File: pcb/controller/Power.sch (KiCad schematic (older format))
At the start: 4 parts

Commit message: controller schematic capture almost done
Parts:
- added C? (x3): 10u, symbol Device:C
- added C?: 47u, symbol Device:C
- added C? (x2): C, symbol Device:C
- added C? (x2): 10n, symbol Device:C
- added C? (x4): 4.7u, symbol Device:C
- added L?: L, symbol Device:L
- added R? (x7): R, symbol Device:R
- added U?: LMZ14201, symbol wbraun_ic_lib:LMZ14201
- added U? (x2): TPS735, symbol wbraun_ic_lib:TPS735
- added U?: TPS82084, symbol wbraun_ic_lib:TPS82084
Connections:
- net at FL?.1: now also J?.1 (Pin_1)
- net at FL?.2: now also C?.1, L?.1
- net at FL?.3: now also J?.2 (Pin_2)
- net GND: now reaches FL?.4
- net GND: now also C?.2, C?.2, C?.1, C?.1, C?.1, C?.1, C?.1, C?.1, C?.1, C?.2, C?.2, C?.2, C?.2, C?.2, R?.1, R?.1, R?.1, R?.2, R?.2, U?.4 (GND), U?.4 (GND), U?.4 (GND), U?.5 (GND), U?.6 (GND), U?.8 (GND), U?.9 (GND), U?.9 (GND), U?.9 (GND)
- net +24V: now reaches C?.1
- net +24V: now also C?.1, L?.2, R?.1, U?.1 (VIN)
- new net: R?.2, U?.2 (RON)
- new net: R?.1, R?.2, U?.3 (EN)
- new net: C?.1, U?.5 (SS)
- new net: C?.2, R?.1, R?.2, U?.6 (FB)
- new net: C?.2, U?.3 (NR/FB) (x2)
- new net: R?.1, R?.2, U?.7 (FB)
- new net +1V0: C?.1, R?.2, U?.8 (VOUT)
- new net +1V8: C?.2, U?.1 (OUT)
- new net +3V3: C?.2, U?.1 (OUT)
- new net +5V: C?.1, C?.1, C?.2, C?.2, U?.1 (EN), U?.3 (VIN), U?.4 (VIN), U?.5 (EN), U?.5 (EN), U?.7 (VOUT), U?.8 (IN), U?.8 (IN)
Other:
- moved on the sheet: C?, FL?

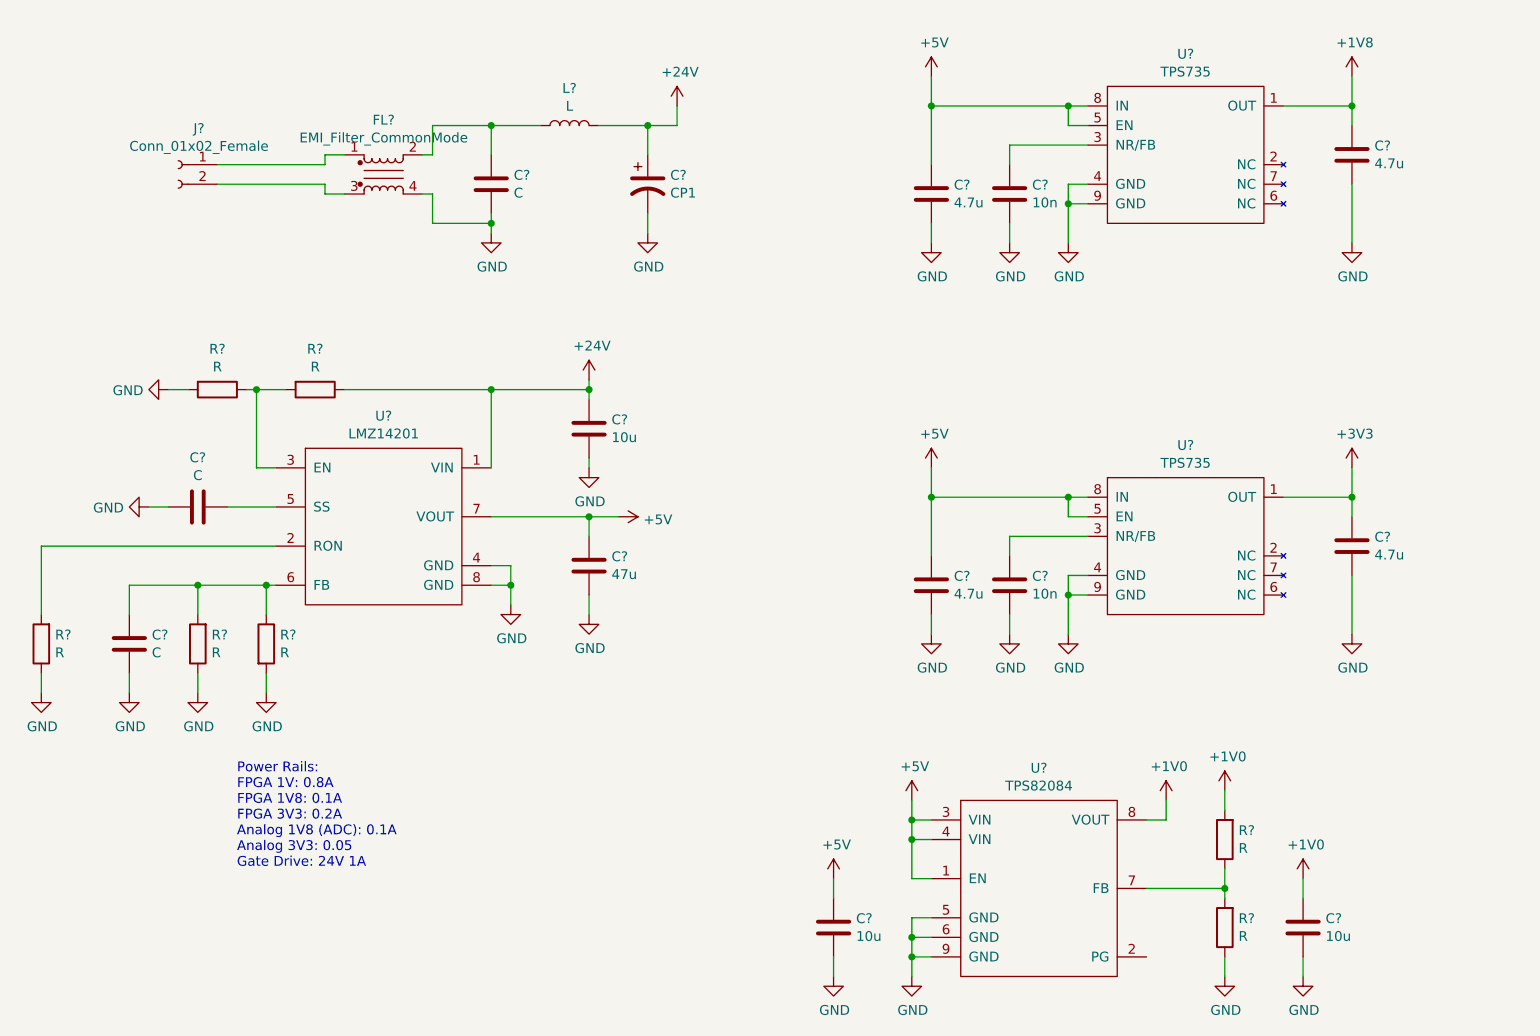
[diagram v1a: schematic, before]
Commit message: started assigning footprints
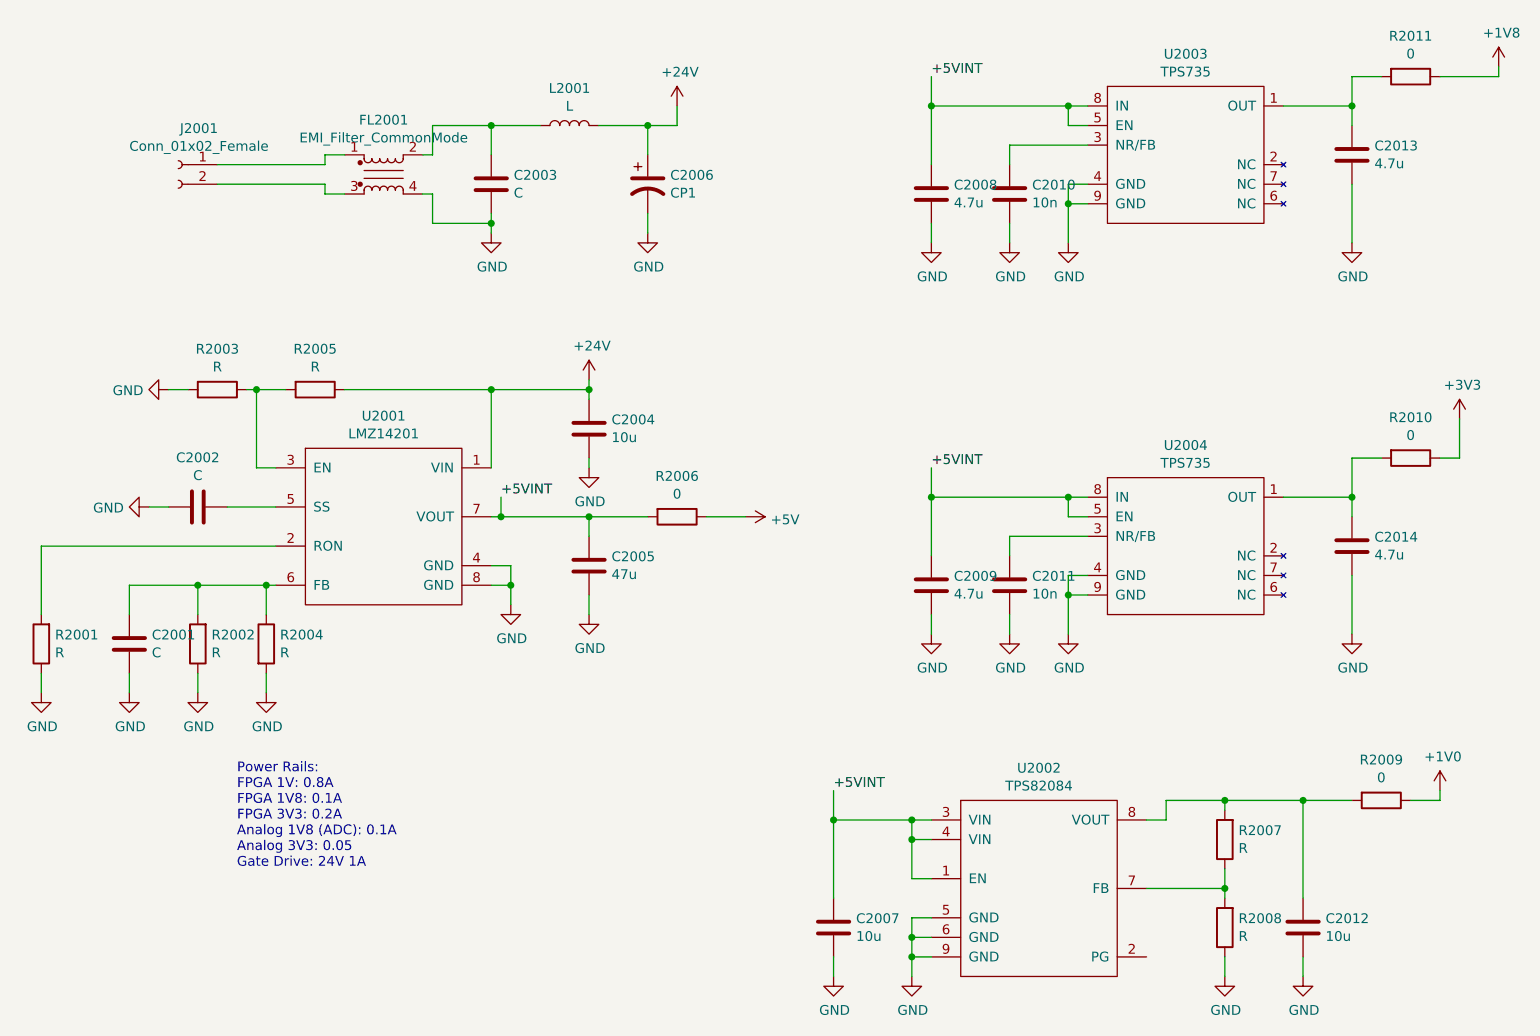
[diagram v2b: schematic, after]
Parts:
- added R2006, R2009, R2010, R2011: 0, symbol Device:R
- C2001, C2002, C2008, C2009, C2010, C2011, C2012, C2013, C2014: renamed from C?; footprint (none) -> Capacitor_SMD:C_0402_1005Metric
- C2004: renamed from C?; footprint (none) -> Capacitor_SMD:C_1206_3216Metric
- C2005, C2007: renamed from C?; footprint (none) -> Capacitor_SMD:C_0805_2012Metric
- gave numbers to parts that had none: 16
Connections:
- net +1V0: now also R2009.1; no longer C2012.1, R2007.2, U2002.8 (VOUT)
- net +1V8: now also R2011.1; no longer C2013.2, U2003.1 (OUT)
- net +3V3: now also R2010.1; no longer C2014.2, U2004.1 (OUT)
- net +5V: now also R2006.1; no longer C2005.1, C2007.1, C2008.2, C2009.2, U2001.7 (VOUT), U2002.1 (EN), U2002.3 (VIN), U2002.4 (VIN), U2003.5 (EN), U2003.8 (IN), U2004.5 (EN), U2004.8 (IN)
- new net: C2013.2, R2011.2, U2003.1 (OUT)
- new net: C2014.2, R2010.2, U2004.1 (OUT)
- new net: C2012.1, R2007.2, R2009.2, U2002.8 (VOUT)
- new net +5VINT: C2005.1, C2007.1, C2008.2, C2009.2, R2006.2, U2001.7 (VOUT), U2002.1 (EN), U2002.3 (VIN), U2002.4 (VIN), U2003.5 (EN), U2003.8 (IN), U2004.5 (EN), U2004.8 (IN)

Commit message: pcb component placement almost done
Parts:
- added C2015: CP2, wbraun_smd:CAP_16mmx37mm_horizontal, symbol Device:CP1
- C2003: footprint (none) -> Capacitor_SMD:C_0805_2012Metric
- C2006: footprint (none) -> Capacitor_THT:CP_Radial_D10.0mm_P5.00mm
- C2012: footprint Capacitor_SMD:C_0402_1005Metric -> Capacitor_SMD:C_0805_2012Metric
- FL2001: footprint (none) -> wbraun_smd:DLW5BTM
- J2001: footprint (none) -> wbraun_smd:TerminalBlock-5.0mm-2
- L2001: footprint (none) -> Inductor_SMD:L_Vishay_IHLP-1212
- R2001, R2002, R2003, R2004, R2005, R2007, R2008: footprint (none) -> Resistor_SMD:R_0402_1005Metric
- R2006, R2009, R2010, R2011: footprint (none) -> Resistor_SMD:R_0805_2012Metric
- U2001: footprint (none) -> wbraun_smd:TO-PMOD-7
- U2002: footprint (none) -> wbraun_smd:uSil-8
- U2003, U2004: footprint (none) -> wbraun_smd:SON-8_EP
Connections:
- net +24V: now also C2015.1
- net +5V: now also C2007.1, C2008.2, C2009.2, U2002.1 (EN), U2002.3 (VIN), U2002.4 (VIN), U2003.5 (EN), U2003.8 (IN), U2004.5 (EN), U2004.8 (IN)
- net +5VINT: now also C2001.1, R2002.1; no longer C2007.1, C2008.2, C2009.2, U2002.1 (EN), U2002.3 (VIN), U2002.4 (VIN), U2003.5 (EN), U2003.8 (IN), U2004.5 (EN), U2004.8 (IN)
- net GND: now also FL2001.3, C2015.2; no longer C2001.1, FL2001.4, R2002.1
- net at FL2001.1: now also C2003.1, L2001.1; no longer J2001.1 (Pin_1)
- net at J2001.2 (Pin_2): now also FL2001.4; no longer FL2001.3
- new net: FL2001.2, J2001.1 (Pin_1)
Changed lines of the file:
@@
 F 0 "FL2001" H 2500 2428 50  0000 C CNN
 F 1 "EMI_Filter_CommonMode" H 2500 2337 50  0000 C CNN
-F 2 "" V 2500 2190 50  0001 C CNN
+F 2 "wbraun_smd:DLW5BTM" V 2500 2190 50  0001 C CNN
 F 3 "~" V 2500 2190 50  0000 C CNN
 	1    2500 2150
-	1    0    0    -1
+	-1   0    0    -1
 $EndComp
 $Comp
@@
 F 0 "J2001" H 1344 2285 50  0000 C CNN
 F 1 "Conn_01x02_Female" H 1344 2194 50  0000 C CNN
-F 2 "" H 1450 2100 50  0001 C CNN
+F 2 "wbraun_smd:TerminalBlock-5.0mm-2" H 1450 2100 50  0001 C CNN
 F 3 "~" H 1450 2100 50  0001 C CNN
 	1    1450 2100
@@
 F 0 "C2003" H 3165 2246 50  0000 L CNN
 F 1 "C" H 3165 2155 50  0000 L CNN
-F 2 "" H 3088 2050 50  0001 C CNN
+F 2 "Capacitor_SMD:C_0805_2012Metric" H 3088 2050 50  0001 C CNN
 F 3 "~" H 3050 2200 50  0001 C CNN
 	1    3050 2200
@@
 F 0 "C2006" H 3965 2246 50  0000 L CNN
 F 1 "CP1" H 3965 2155 50  0000 L CNN
-F 2 "" H 3850 2200 50  0001 C CNN
+F 2 "Capacitor_THT:CP_Radial_D10.0mm_P5.00mm" H 3850 2200 50  0001 C CNN
 F 3 "~" H 3850 2200 50  0001 C CNN
 	1    3850 2200
@@
 F 0 "L2001" V 3640 1900 50  0000 C CNN
 F 1 "L" V 3549 1900 50  0000 C CNN
-F 2 "" H 3450 1900 50  0001 C CNN
+F 2 "Inductor_SMD:L_Vishay_IHLP-1212" H 3450 1900 50  0001 C CNN
 F 3 "~" H 3450 1900 50  0001 C CNN
 	1    3450 1900
@@
 F 0 "U2001" H 2500 4515 50  0000 C CNN
 F 1 "LMZ14201" H 2500 4424 50  0000 C CNN
-F 2 "" H 2100 3750 50  0001 C CNN
+F 2 "wbraun_smd:TO-PMOD-7" H 2100 3750 50  0001 C CNN
 F 3 "" H 2100 3750 50  0001 C CNN
 	1    2500 3950
@@
 F 0 "R2002" H 1480 4504 50  0000 R CNN
 F 1 "R" H 1480 4595 50  0000 R CNN
-F 2 "" V 1480 4550 50  0001 C CNN
+F 2 "Resistor_SMD:R_0402_1005Metric" V 1480 4550 50  0001 C CNN
 F 3 "~" H 1550 4550 50  0001 C CNN
 	1    1550 4550
@@
 F 0 "R2004" H 1970 4596 50  0000 L CNN
 F 1 "R" H 1970 4505 50  0000 L CNN
-F 2 "" V 1830 4550 50  0001 C CNN
+F 2 "Resistor_SMD:R_0402_1005Metric" V 1830 4550 50  0001 C CNN
 F 3 "~" H 1900 4550 50  0001 C CNN
 	1    1900 4550
@@
 F 0 "R2005" V 1943 3250 50  0000 C CNN
 F 1 "R" V 2034 3250 50  0000 C CNN
-F 2 "" V 2080 3250 50  0001 C CNN
+F 2 "Resistor_SMD:R_0402_1005Metric" V 2080 3250 50  0001 C CNN
 F 3 "~" H 2150 3250 50  0001 C CNN
 	1    2150 3250
@@
 F 0 "R2003" V 1443 3250 50  0000 C CNN
 F 1 "R" V 1534 3250 50  0000 C CNN
-F 2 "" V 1580 3250 50  0001 C CNN
+F 2 "Resistor_SMD:R_0402_1005Metric" V 1580 3250 50  0001 C CNN
 F 3 "~" H 1650 3250 50  0001 C CNN
 	1    1650 3250
@@
 F 0 "R2001" H 680 4504 50  0000 R CNN
 F 1 "R" H 680 4595 50  0000 R CNN
-F 2 "" V 680 4550 50  0001 C CNN
+F 2 "Resistor_SMD:R_0402_1005Metric" V 680 4550 50  0001 C CNN
 F 3 "~" H 750 4550 50  0001 C CNN
 	1    750  4550
@@
 $EndComp
 $Comp
-L power:GND #PWR0111
-U 1 1 5C6A74F1
-P 1200 4800
-F 0 "#PWR0111" H 1200 4550 50  0001 C CNN
-F 1 "GND" H 1205 4627 50  0000 C CNN
-F 2 "" H 1200 4800 50  0001 C CNN
-F 3 "" H 1200 4800 50  0001 C CNN
-	1    1200 4800
-	1    0    0    -1
-$EndComp
-$Comp
-L power:GND #PWR0112
-U 1 1 5C6A751A
-P 1550 4800
-F 0 "#PWR0112" H 1550 4550 50  0001 C CNN
-F 1 "GND" H 1555 4627 50  0000 C CNN
-F 2 "" H 1550 4800 50  0001 C CNN
-F 3 "" H 1550 4800 50  0001 C CNN
-	1    1550 4800
-	1    0    0    -1
-$EndComp
-$Comp
 L power:GND #PWR0113
 U 1 1 5C6A7543
@@
 F 0 "U2003" H 6600 2565 50  0000 C CNN
 F 1 "TPS735" H 6600 2474 50  0000 C CNN
-F 2 "" H 7300 1800 50  0001 C CNN
+F 2 "wbraun_smd:SON-8_EP" H 7300 1800 50  0001 C CNN
 F 3 "" H 7300 1800 50  0001 C CNN
 	1    6600 2050
@@
 F 0 "U2004" H 6600 4565 50  0000 C CNN
 F 1 "TPS735" H 6600 4474 50  0000 C CNN
-F 2 "" H 7300 3800 50  0001 C CNN
+F 2 "wbraun_smd:SON-8_EP" H 7300 3800 50  0001 C CNN
 F 3 "" H 7300 3800 50  0001 C CNN
 	1    6600 4050
@@
 F 0 "U2002" H 5850 6415 50  0000 C CNN
 F 1 "TPS82084" H 5850 6324 50  0000 C CNN
-F 2 "" H 5800 5800 50  0001 C CNN
+F 2 "wbraun_smd:uSil-8" H 5800 5800 50  0001 C CNN
 F 3 "" H 5800 5800 50  0001 C CNN
 	1    5850 5800
@@
 F 0 "C2012" H 7315 6046 50  0000 L CNN
 F 1 "10u" H 7315 5955 50  0000 L CNN
-F 2 "Capacitor_SMD:C_0402_1005Metric" H 7238 5850 50  0001 C CNN
+F 2 "Capacitor_SMD:C_0805_2012Metric" H 7238 5850 50  0001 C CNN
 F 3 "~" H 7200 6000 50  0001 C CNN
 	1    7200 6000
@@
 F 0 "R2007" H 6730 5504 50  0000 R CNN
 F 1 "R" H 6730 5595 50  0000 R CNN
-F 2 "" V 6730 5550 50  0001 C CNN
+F 2 "Resistor_SMD:R_0402_1005Metric" V 6730 5550 50  0001 C CNN
 F 3 "~" H 6800 5550 50  0001 C CNN
 	1    6800 5550
@@
 F 0 "R2008" H 6730 5954 50  0000 R CNN
 F 1 "R" H 6730 6045 50  0000 R CNN
-F 2 "" V 6730 6000 50  0001 C CNN
+F 2 "Resistor_SMD:R_0402_1005Metric" V 6730 6000 50  0001 C CNN
 F 3 "~" H 6800 6000 50  0001 C CNN
 	1    6800 6000
@@
 F 0 "R2006" V 3793 3900 50  0000 C CNN
 F 1 "0" V 3884 3900 50  0000 C CNN
-F 2 "" V 3930 3900 50  0001 C CNN
+F 2 "Resistor_SMD:R_0805_2012Metric" V 3930 3900 50  0001 C CNN
 F 3 "~" H 4000 3900 50  0001 C CNN
 	1    4000 3900
@@
 	4800 5450 4800 5300
 Connection ~ 4800 5450
-Text Label 4800 5300 0    50   ~ 0
-+5VINT
-Text Label 5300 3650 0    50   ~ 0
-+5VINT
-Text Label 5300 1650 0    50   ~ 0
-+5VINT
 $Comp
 L Device:R R2011
@@
 F 0 "R2011" V 7543 1650 50  0000 C CNN
 F 1 "0" V 7634 1650 50  0000 C CNN
-F 2 "" V 7680 1650 50  0001 C CNN
+F 2 "Resistor_SMD:R_0805_2012Metric" V 7680 1650 50  0001 C CNN
 F 3 "~" H 7750 1650 50  0001 C CNN
 	1    7750 1650
@@
 F 0 "R2010" V 7543 3600 50  0000 C CNN
 F 1 "0" V 7634 3600 50  0000 C CNN
-F 2 "" V 7680 3600 50  0001 C CNN
+F 2 "Resistor_SMD:R_0805_2012Metric" V 7680 3600 50  0001 C CNN
 F 3 "~" H 7750 3600 50  0001 C CNN
 	1    7750 3600
@@
 F 0 "R2009" V 7393 5350 50  0000 C CNN
 F 1 "0" V 7484 5350 50  0000 C CNN
-F 2 "" V 7530 5350 50  0001 C CNN
+F 2 "Resistor_SMD:R_0805_2012Metric" V 7530 5350 50  0001 C CNN
 F 3 "~" H 7600 5350 50  0001 C CNN
 	1    7600 5350
@@
 Wire Wire Line
 	8200 1650 7900 1650
+Text Label 1200 4800 0    50   ~ 0
++5VINT
+Text Label 1550 4800 0    50   ~ 0
++5VINT
+$Comp
+L Device:CP1 C2015
+U 1 1 5C5EEDC0
+P 4350 2200
+F 0 "C2015" H 4465 2246 50  0000 L CNN
+F 1 "CP2" H 4465 2155 50  0000 L CNN
+F 2 "wbraun_smd:CAP_16mmx37mm_horizontal" H 4350 2200 50  0001 C CNN
+F 3 "~" H 4350 2200 50  0001 C CNN
+	1    4350 2200
+	1    0    0    -1
+$EndComp
+$Comp
+L power:GND #PWR0157
+U 1 1 5C5EEE47
+P 4350 2450
+F 0 "#PWR0157" H 4350 2200 50  0001 C CNN
+F 1 "GND" H 4355 2277 50  0000 C CNN
+F 2 "" H 4350 2450 50  0001 C CNN
+F 3 "" H 4350 2450 50  0001 C CNN
+	1    4350 2450
+	1    0    0    -1
+$EndComp
+Wire Wire Line
+	4000 1900 4350 1900
+Wire Wire Line
+	4350 1900 4350 2050
+Connection ~ 4000 1900
+Wire Wire Line
+	4350 2350 4350 2450
+$Comp
+L power:+5V #PWR0158
+U 1 1 5C5F8ADB
+P 5300 1650
+F 0 "#PWR0158" H 5300 1500 50  0001 C CNN
+F 1 "+5V" V 5315 1778 50  0000 L CNN
+F 2 "" H 5300 1650 50  0001 C CNN
+F 3 "" H 5300 1650 50  0001 C CNN
+	1    5300 1650
+	1    0    0    -1
+$EndComp
+$Comp
+L power:+5V #PWR0159
+U 1 1 5C5F8BCD
+P 5300 3650
+F 0 "#PWR0159" H 5300 3500 50  0001 C CNN
+F 1 "+5V" V 5315 3778 50  0000 L CNN
+F 2 "" H 5300 3650 50  0001 C CNN
+F 3 "" H 5300 3650 50  0001 C CNN
+	1    5300 3650
+	1    0    0    -1
+$EndComp
+$Comp
+L power:+5V #PWR0166
+U 1 1 5C5F8C1A
+P 4800 5300
+F 0 "#PWR0166" H 4800 5150 50  0001 C CNN
+F 1 "+5V" V 4815 5428 50  0000 L CNN
+F 2 "" H 4800 5300 50  0001 C CNN
+F 3 "" H 4800 5300 50  0001 C CNN
+	1    4800 5300
+	1    0    0    -1
+$EndComp
 $EndSCHEMATC

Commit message: controller PCB routing progress
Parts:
- added C2016: 47u, Capacitor_SMD:C_0805_2012Metric, symbol Device:C
- J2001: footprint wbraun_smd:TerminalBlock-5.0mm-2 -> wbraun_smd:Terminal-block-plug_2x1_3.5mm-pitch
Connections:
- net +5V: now also C2016.1
- net GND: now also C2016.2
- net at FL2001.2: now also J2001.2 (Pin_2); no longer J2001.1 (Pin_1)
- net at FL2001.4: now also J2001.1 (Pin_1); no longer J2001.2 (Pin_2)
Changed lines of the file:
@@
 L Connector:Conn_01x02_Female J2001
 U 1 1 5C45A3A4
-P 1450 2100
-F 0 "J2001" H 1344 2285 50  0000 C CNN
-F 1 "Conn_01x02_Female" H 1344 2194 50  0000 C CNN
-F 2 "wbraun_smd:TerminalBlock-5.0mm-2" H 1450 2100 50  0001 C CNN
-F 3 "~" H 1450 2100 50  0001 C CNN
-	1    1450 2100
-	-1   0    0    -1
+P 1450 2200
+F 0 "J2001" H 1344 2385 50  0000 C CNN
+F 1 "Conn_01x02_Female" H 1344 2294 50  0000 C CNN
+F 2 "wbraun_smd:Terminal-block-plug_2x1_3.5mm-pitch" H 1450 2200 50  0001 C CNN
+F 3 "~" H 1450 2200 50  0001 C CNN
+	1    1450 2200
+	-1   0    0    1
 $EndComp
 $Comp
@@
 	3550 3900 3850 3900
 Wire Wire Line
-	4150 3900 4350 3900
+	4150 3900 4250 3900
 Wire Wire Line
 	3100 3800 3100 3900
@@
 	1    0    0    -1
 $EndComp
+$Comp
+L Device:C C2016
+U 1 1 5C45724D
+P 4250 4150
+F 0 "C2016" H 4365 4196 50  0000 L CNN
+F 1 "47u" H 4365 4105 50  0000 L CNN
+F 2 "Capacitor_SMD:C_0805_2012Metric" H 4288 4000 50  0001 C CNN
+F 3 "~" H 4250 4150 50  0001 C CNN
+	1    4250 4150
+	1    0    0    -1
+$EndComp
+Wire Wire Line
+	4250 3900 4250 4000
+$Comp
+L power:GND #PWR0195
+U 1 1 5C457255
+P 4250 4400
+F 0 "#PWR0195" H 4250 4150 50  0001 C CNN
+F 1 "GND" H 4255 4227 50  0000 C CNN
+F 2 "" H 4250 4400 50  0001 C CNN
+F 3 "" H 4250 4400 50  0001 C CNN
+	1    4250 4400
+	1    0    0    -1
+$EndComp
+Wire Wire Line
+	4250 4300 4250 4400
+Connection ~ 4250 3900
+Wire Wire Line
+	4250 3900 4350 3900
 $EndSCHEMATC

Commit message: controller layout done and schematic reviewed
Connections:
- net +24V: now also R2001.1
- net GND: no longer R2001.1
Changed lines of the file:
@@
 	1950 4050 750  4050
-$Comp
-L power:GND #PWR0110
-U 1 1 5C6A749B
-P 750 4800
-F 0 "#PWR0110" H 750 4550 50  0001 C CNN
-F 1 "GND" H 755 4627 50  0000 C CNN
-F 2 "" H 750 4800 50  0001 C CNN
-F 3 "" H 750 4800 50  0001 C CNN
-	1    750  4800
-	1    0    0    -1
-$EndComp
 $Comp
 L power:GND #PWR0113
@@
 Wire Wire Line
 	4250 3900 4350 3900
+$Comp
+L power:+24V #PWR0110
+U 1 1 5C4E5B6C
+P 750 4800
+F 0 "#PWR0110" H 750 4650 50  0001 C CNN
+F 1 "+24V" H 765 4973 50  0000 C CNN
+F 2 "" H 750 4800 50  0001 C CNN
+F 3 "" H 750 4800 50  0001 C CNN
+	1    750  4800
+	-1   0    0    1
+$EndComp
 $EndSCHEMATC
